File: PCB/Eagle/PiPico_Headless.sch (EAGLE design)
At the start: 14 parts, among them U1 RASPBERRY_PICOTH, X1 TOBU3, X2 TOBU3, X3 TOBU3

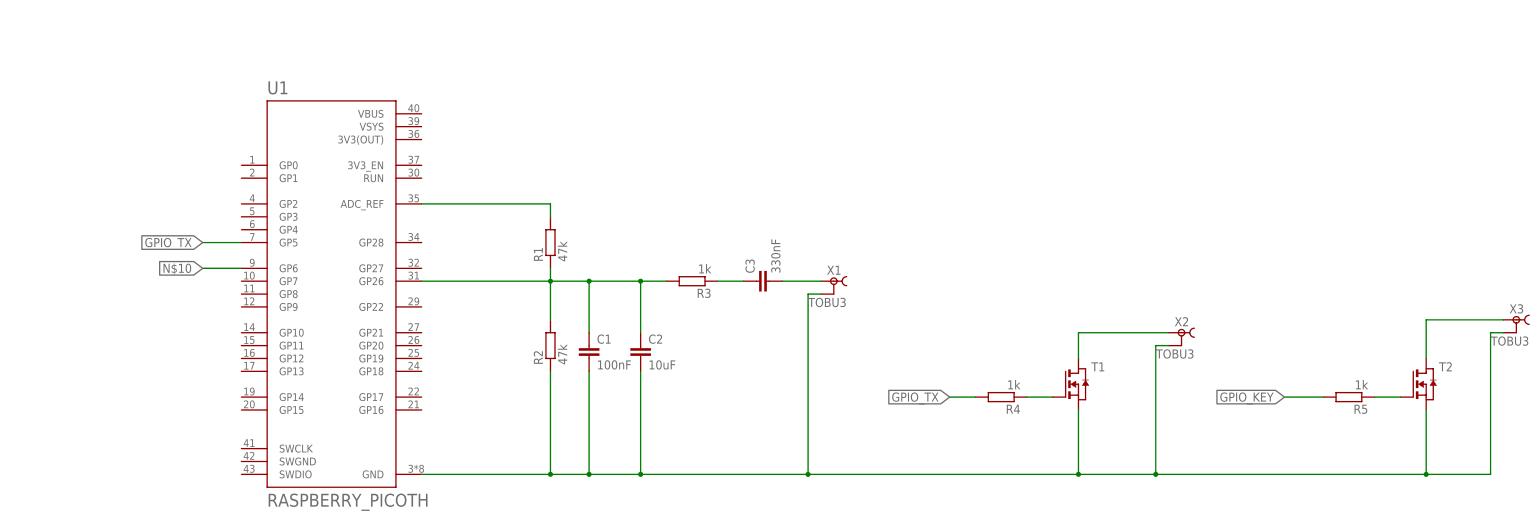
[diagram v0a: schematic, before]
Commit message: Fixed a FIFO race condition
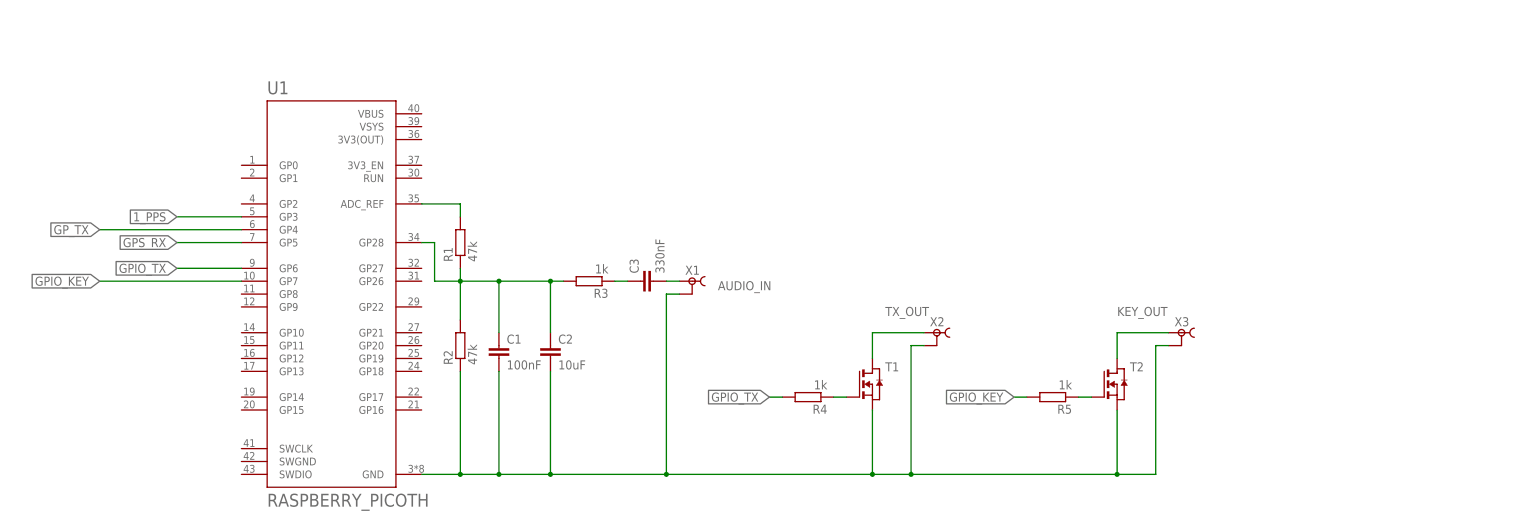
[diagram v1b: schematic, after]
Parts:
- X1: value TOBU3 -> AUDIO_IN
- X2: value TOBU3 -> TX_OUT
- X3: value TOBU3 -> KEY_OUT
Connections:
- removed net N$10: U1.GP6
- new net 1_PPS: U1.GP3
- new net GPS_RX: U1.GP5
- new net GP_TX: U1.GP4
- net GPIO_KEY: now also U1.GP7
- net GPIO_TX: now also U1.GP6; no longer U1.GP5
- net N$1: now also U1.GP28; no longer U1.GP26
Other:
- moved on the sheet: C1, C2, C3, R1, R2, R3, R4, R5, T1, T2, X1, X2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

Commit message: V1.0 PCB
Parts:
- added C4, C5: 100nF, resistor:C-EUC0805
- added U$1: GPS, gps:GPS
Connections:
- removed net GP_TX: U1.GP4
- new net 3V3: U$1.VCC, U1.3V3(OUT)
- new net GPS_TX: U$1.TXD, U1.GP4
- net 1_PPS: now also U$1.1_PPS
- net GND: now also C4.1, C5.1, U$1.GND
- net GPS_RX: now also U$1.RXD
- net N$8: now also C4.2
- net N$9: now also C5.2
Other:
- moved on the sheet: R4, T1, X3
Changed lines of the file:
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@@
 <part name="R4" library="resistor" deviceset="R-EU_" device="R0805" value="1k"/>
 <part name="R5" library="resistor" deviceset="R-EU_" device="R0805" value="1k"/>
+<part name="U$1" library="gps" deviceset="GPS" device=""/>
+<part name="C4" library="resistor" deviceset="C-EU" device="C0805" value="100nF"/>
+<part name="C5" library="resistor" deviceset="C-EU" device="C0805" value="100nF"/>
 </parts>
 <sheets>
@@
 <attribute name="VALUE" x="167.64" y="45.72" size="1.778" layer="96" rot="MR180"/>
 </instance>
-<instance part="X3" gate="B" x="226.06" y="40.64" smashed="yes" rot="MR0">
-<attribute name="NAME" x="227.584" y="41.91" size="1.778" layer="95" rot="MR0"/>
-<attribute name="VALUE" x="213.36" y="45.72" size="1.778" layer="96" rot="MR180"/>
-</instance>
-<instance part="T1" gate="A" x="165.1" y="30.48"/>
+<instance part="X3" gate="B" x="231.14" y="40.64" smashed="yes" rot="MR0">
+<attribute name="NAME" x="232.664" y="41.91" size="1.778" layer="95" rot="MR0"/>
+<attribute name="VALUE" x="218.44" y="45.72" size="1.778" layer="96" rot="MR180"/>
+</instance>
+<instance part="T1" gate="A" x="162.56" y="33.02"/>
 <instance part="T2" gate="A" x="213.36" y="30.48"/>
-<instance part="R4" gate="G$1" x="152.4" y="27.94" rot="R180"/>
+<instance part="R4" gate="G$1" x="149.86" y="27.94" rot="R180"/>
 <instance part="R5" gate="G$1" x="200.66" y="27.94" rot="R180"/>
+<instance part="U$1" gate="G$1" x="170.18" y="88.9"/>
+<instance part="C4" gate="G$1" x="170.18" y="20.32" smashed="yes" rot="R180">
+<attribute name="NAME" x="176.784" y="18.161" size="1.778" layer="95"/>
+<attribute name="VALUE" x="176.784" y="20.701" size="1.778" layer="96"/>
+</instance>
+<instance part="C5" gate="G$1" x="220.98" y="20.32" smashed="yes" rot="R180">
+<attribute name="NAME" x="227.584" y="18.161" size="1.778" layer="95"/>
+<attribute name="VALUE" x="227.584" y="20.701" size="1.778" layer="96"/>
+</instance>
 </instances>
 <busses>
@@
 <wire x1="124.46" y1="12.7" x2="101.6" y2="12.7" width="0.1524" layer="91"/>
 <pinref part="T2" gate="A" pin="S"/>
-<wire x1="124.46" y1="12.7" x2="165.1" y2="12.7" width="0.1524" layer="91"/>
-<wire x1="165.1" y1="12.7" x2="172.72" y2="12.7" width="0.1524" layer="91"/>
-<wire x1="172.72" y1="12.7" x2="213.36" y2="12.7" width="0.1524" layer="91"/>
+<wire x1="124.46" y1="12.7" x2="162.56" y2="12.7" width="0.1524" layer="91"/>
+<wire x1="162.56" y1="12.7" x2="170.18" y2="12.7" width="0.1524" layer="91"/>
+<wire x1="170.18" y1="12.7" x2="175.26" y2="12.7" width="0.1524" layer="91"/>
+<wire x1="175.26" y1="12.7" x2="213.36" y2="12.7" width="0.1524" layer="91"/>
 <wire x1="213.36" y1="12.7" x2="213.36" y2="25.4" width="0.1524" layer="91"/>
 <pinref part="T1" gate="A" pin="S"/>
-<wire x1="165.1" y1="25.4" x2="165.1" y2="12.7" width="0.1524" layer="91"/>
+<wire x1="162.56" y1="27.94" x2="162.56" y2="12.7" width="0.1524" layer="91"/>
 <pinref part="X2" gate="B" pin="2"/>
-<wire x1="175.26" y1="38.1" x2="172.72" y2="38.1" width="0.1524" layer="91"/>
-<wire x1="172.72" y1="38.1" x2="172.72" y2="12.7" width="0.1524" layer="91"/>
+<wire x1="175.26" y1="38.1" x2="175.26" y2="12.7" width="0.1524" layer="91"/>
 <pinref part="X3" gate="B" pin="2"/>
-<wire x1="223.52" y1="38.1" x2="220.98" y2="38.1" width="0.1524" layer="91"/>
-<wire x1="220.98" y1="38.1" x2="220.98" y2="12.7" width="0.1524" layer="91"/>
+<wire x1="228.6" y1="38.1" x2="226.06" y2="38.1" width="0.1524" layer="91"/>
+<wire x1="226.06" y1="38.1" x2="226.06" y2="12.7" width="0.1524" layer="91"/>
+<wire x1="226.06" y1="12.7" x2="220.98" y2="12.7" width="0.1524" layer="91"/>
+<junction x="162.56" y="12.7"/>
+<junction x="213.36" y="12.7"/>
+<junction x="175.26" y="12.7"/>
+<junction x="124.46" y="12.7"/>
+<pinref part="C4" gate="G$1" pin="1"/>
 <wire x1="220.98" y1="12.7" x2="213.36" y2="12.7" width="0.1524" layer="91"/>
-<junction x="165.1" y="12.7"/>
-<junction x="213.36" y="12.7"/>
-<junction x="172.72" y="12.7"/>
-<junction x="124.46" y="12.7"/>
+<wire x1="170.18" y1="17.78" x2="170.18" y2="12.7" width="0.1524" layer="91"/>
+<junction x="170.18" y="12.7"/>
+<pinref part="C5" gate="G$1" pin="1"/>
+<wire x1="220.98" y1="17.78" x2="220.98" y2="12.7" width="0.1524" layer="91"/>
+<junction x="220.98" y="12.7"/>
+</segment>
+<segment>
+<pinref part="U$1" gate="G$1" pin="GND"/>
+<wire x1="157.48" y1="86.36" x2="132.08" y2="86.36" width="0.1524" layer="91"/>
+<label x="132.08" y="86.36" size="1.778" layer="95" rot="R180" xref="yes"/>
 </segment>
 </net>
@@
 <pinref part="R4" gate="G$1" pin="1"/>
 <pinref part="T1" gate="A" pin="G"/>
-<wire x1="157.48" y1="27.94" x2="160.02" y2="27.94" width="0.1524" layer="91"/>
+<wire x1="154.94" y1="27.94" x2="157.48" y2="30.48" width="0.1524" layer="91"/>
 </segment>
 </net>
@@
 <segment>
 <pinref part="T1" gate="A" pin="D"/>
-<wire x1="165.1" y1="35.56" x2="165.1" y2="40.64" width="0.1524" layer="91"/>
+<wire x1="162.56" y1="38.1" x2="162.56" y2="40.64" width="0.1524" layer="91"/>
 <pinref part="X2" gate="B" pin="1"/>
-<wire x1="165.1" y1="40.64" x2="175.26" y2="40.64" width="0.1524" layer="91"/>
+<wire x1="162.56" y1="40.64" x2="170.18" y2="40.64" width="0.1524" layer="91"/>
+<pinref part="C4" gate="G$1" pin="2"/>
+<wire x1="170.18" y1="40.64" x2="175.26" y2="40.64" width="0.1524" layer="91"/>
+<wire x1="170.18" y1="25.4" x2="170.18" y2="40.64" width="0.1524" layer="91"/>
+<junction x="170.18" y="40.64"/>
 </segment>
 </net>
@@
 <wire x1="213.36" y1="35.56" x2="213.36" y2="40.64" width="0.1524" layer="91"/>
 <pinref part="X3" gate="B" pin="1"/>
-<wire x1="213.36" y1="40.64" x2="223.52" y2="40.64" width="0.1524" layer="91"/>
+<wire x1="213.36" y1="40.64" x2="220.98" y2="40.64" width="0.1524" layer="91"/>
+<pinref part="C5" gate="G$1" pin="2"/>
+<wire x1="220.98" y1="40.64" x2="228.6" y2="40.64" width="0.1524" layer="91"/>
+<wire x1="220.98" y1="25.4" x2="220.98" y2="40.64" width="0.1524" layer="91"/>
+<junction x="220.98" y="40.64"/>
 </segment>
 </net>
@@
 <segment>
 <pinref part="R4" gate="G$1" pin="2"/>
-<wire x1="147.32" y1="27.94" x2="144.78" y2="27.94" width="0.1524" layer="91"/>
-<label x="144.78" y="27.94" size="1.778" layer="95" rot="R180" xref="yes"/>
+<wire x1="144.78" y1="27.94" x2="139.7" y2="27.94" width="0.1524" layer="91"/>
+<label x="139.7" y="27.94" size="1.778" layer="95" rot="R180" xref="yes"/>
 </segment>
 <segment>
@@
 <label x="27.94" y="58.42" size="1.778" layer="95" rot="R180" xref="yes"/>
 </segment>
+<segment>
+<pinref part="U$1" gate="G$1" pin="RXD"/>
+<wire x1="157.48" y1="88.9" x2="147.32" y2="88.9" width="0.1524" layer="91"/>
+<label x="147.32" y="88.9" size="1.778" layer="95" rot="R180" xref="yes"/>
+</segment>
 </net>
 <net name="1_PPS" class="0">
@@
 <label x="27.94" y="63.5" size="1.778" layer="95" rot="R180" xref="yes"/>
 </segment>
-</net>
-<net name="GP_TX" class="0">
+<segment>
+<pinref part="U$1" gate="G$1" pin="1_PPS"/>
+<wire x1="157.48" y1="93.98" x2="147.32" y2="93.98" width="0.1524" layer="91"/>
+<label x="147.32" y="93.98" size="1.778" layer="95" rot="R180" xref="yes"/>
+</segment>
+</net>
+<net name="GPS_TX" class="0">
+<segment>
+<pinref part="U$1" gate="G$1" pin="TXD"/>
+<wire x1="157.48" y1="91.44" x2="132.08" y2="91.44" width="0.1524" layer="91"/>
+<label x="132.08" y="91.44" size="1.778" layer="95" rot="R180" xref="yes"/>
+</segment>
 <segment>
 <pinref part="U1" gate="U$1" pin="GP4"/>
@@
 </segment>
 </net>
+<net name="3V3" class="0">
+<segment>
+<pinref part="U$1" gate="G$1" pin="VCC"/>
+<wire x1="157.48" y1="83.82" x2="147.32" y2="83.82" width="0.1524" layer="91"/>
+<label x="147.32" y="83.82" size="1.778" layer="95" rot="R180" xref="yes"/>
+</segment>
+<segment>
+<pinref part="U1" gate="U$1" pin="3V3(OUT)"/>
+<wire x1="76.2" y1="78.74" x2="91.44" y2="78.74" width="0.1524" layer="91"/>
+<label x="91.44" y="78.74" size="1.778" layer="95" xref="yes"/>
+</segment>
+</net>

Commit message: Updated PCB
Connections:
- net GPS_RX: now also U$1.TXD; no longer U$1.RXD
- net GPS_TX: now also U$1.RXD; no longer U$1.TXD
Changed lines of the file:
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@@
 </segment>
 <segment>
-<pinref part="U$1" gate="G$1" pin="RXD"/>
-<wire x1="157.48" y1="88.9" x2="147.32" y2="88.9" width="0.1524" layer="91"/>
-<label x="147.32" y="88.9" size="1.778" layer="95" rot="R180" xref="yes"/>
+<pinref part="U$1" gate="G$1" pin="TXD"/>
+<wire x1="157.48" y1="91.44" x2="132.08" y2="91.44" width="0.1524" layer="91"/>
+<label x="132.08" y="91.44" size="1.778" layer="95" rot="R180" xref="yes"/>
 </segment>
 </net>
@@
 <net name="GPS_TX" class="0">
 <segment>
-<pinref part="U$1" gate="G$1" pin="TXD"/>
-<wire x1="157.48" y1="91.44" x2="132.08" y2="91.44" width="0.1524" layer="91"/>
-<label x="132.08" y="91.44" size="1.778" layer="95" rot="R180" xref="yes"/>
-</segment>
-<segment>
 <pinref part="U1" gate="U$1" pin="GP4"/>
 <wire x1="40.64" y1="60.96" x2="12.7" y2="60.96" width="0.1524" layer="91"/>
 <label x="12.7" y="60.96" size="1.778" layer="95" rot="R180" xref="yes"/>
 </segment>
+<segment>
+<pinref part="U$1" gate="G$1" pin="RXD"/>
+<wire x1="157.48" y1="88.9" x2="147.32" y2="88.9" width="0.1524" layer="91"/>
+<label x="147.32" y="88.9" size="1.778" layer="95" rot="R180" xref="yes"/>
+</segment>
 </net>
